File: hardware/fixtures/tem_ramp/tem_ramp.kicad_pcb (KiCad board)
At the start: 2 copper layers, 100 x 59 mm, 0 parts

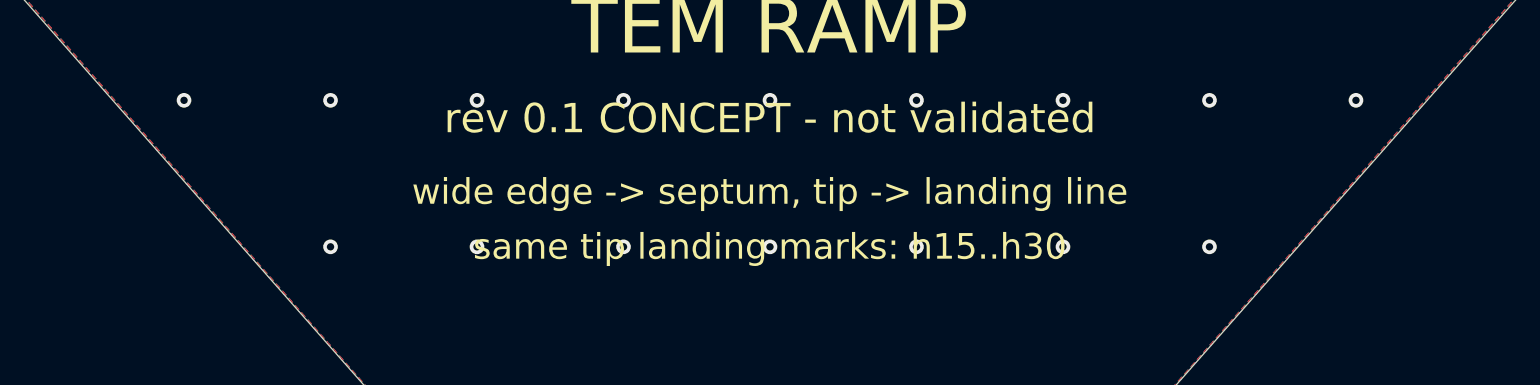
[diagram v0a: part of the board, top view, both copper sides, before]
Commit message: First fixture session: TEM cell sees the implant at every placement
TEM cell (h = 20 mm): the implanted Nano X shows a ~1 dB, ~40 MHz wide
notch at 1171 MHz at every placement and both orientations (sim: -1.2 dB
at 1185 MHz). Six of seven genuine placements stay within 0.2 dB; one
genuine re-check showed a similar notch near 1230 MHz, cause unknown.
Slot line: a small (-0.13..-0.20 dB) dip at 817-861 MHz at 0 deg only.

Also:
- gen_fixtures.py: TEM landing marks now place the ramp tip where the
  rigid ramp's tab actually lands, with the ramp overlapping the septum by
  4 mm; regenerated TEM boards and assembly step 3.
- nanovna_capture.py: zeros mean "outside the active calibration's span"
  (e.g. slot 1 recalled at power-on); say to `recall 0`.

Co-Authored-By: Claude Opus 5.5 <noreply@anthropic.com>
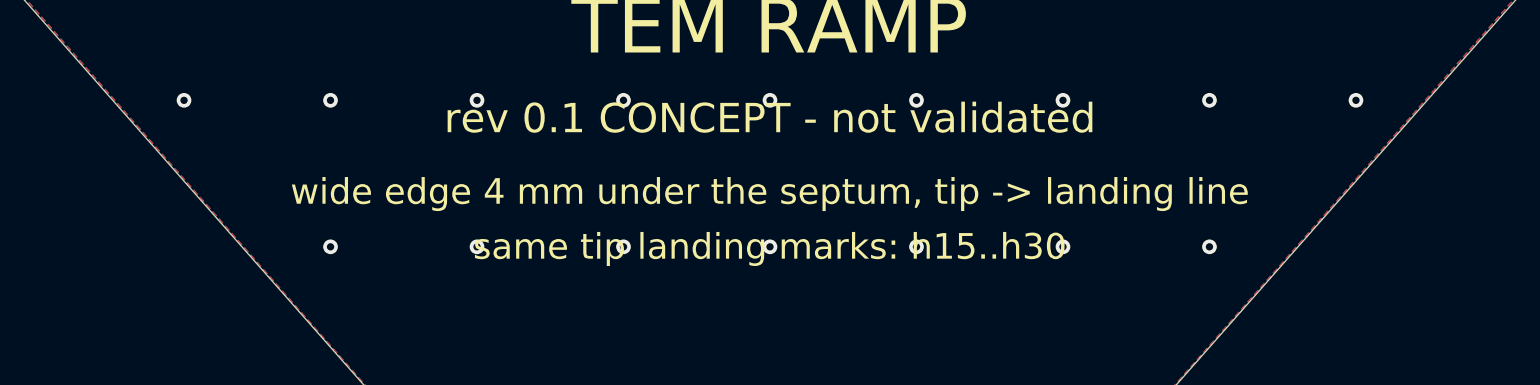
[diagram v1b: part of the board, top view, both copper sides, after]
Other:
- board text added: "wide edge 4 mm under the septum, tip -> landing line"
- board text removed: "wide edge -> septum, tip -> landing line"
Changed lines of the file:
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@@
 		(layer "Edge.Cuts")
 	)
-	(gr_text "wide edge -> septum, tip -> landing line"
+	(gr_text "wide edge 4 mm under the septum, tip -> landing line"
 		(at 150 171 0)
 		(layer "F.SilkS")
@@
 	)
 	(via
+		(at 158 174)
+		(size 0.8)
+		(drill 0.4)
+		(layers "F.Cu" "B.Cu")
+		(net "SEPTUM")
+	)
+	(via
+		(at 150 174)
+		(size 0.8)
+		(drill 0.4)
+		(layers "F.Cu" "B.Cu")
+		(net "SEPTUM")
+	)
+	(via
+		(at 126 158)
+		(size 0.8)
+		(drill 0.4)
+		(layers "F.Cu" "B.Cu")
+		(net "SEPTUM")
+	)
+	(via
+		(at 166 166)
+		(size 0.8)
+		(drill 0.4)
+		(layers "F.Cu" "B.Cu")
+		(net "SEPTUM")
+	)
+	(via
+		(at 166 182)
+		(size 0.8)
+		(drill 0.4)
+		(layers "F.Cu" "B.Cu")
+		(net "SEPTUM")
+	)
+	(via
+		(at 166 158)
+		(size 0.8)
+		(drill 0.4)
+		(layers "F.Cu" "B.Cu")
+		(net "SEPTUM")
+	)
+	(via
+		(at 158 166)
+		(size 0.8)
+		(drill 0.4)
+		(layers "F.Cu" "B.Cu")
+		(net "SEPTUM")
+	)
+	(via
+		(at 182 158)
+		(size 0.8)
+		(drill 0.4)
+		(layers "F.Cu" "B.Cu")
+		(net "SEPTUM")
+	)
+	(via
 		(at 126 174)
 		(size 0.8)
@@
 	)
 	(via
-		(at 182 158)
+		(at 134 182)
+		(size 0.8)
+		(drill 0.4)
+		(layers "F.Cu" "B.Cu")
+		(net "SEPTUM")
+	)
+	(via
+		(at 118 158)
+		(size 0.8)
+		(drill 0.4)
+		(layers "F.Cu" "B.Cu")
+		(net "SEPTUM")
+	)
+	(via
+		(at 190 158)
+		(size 0.8)
+		(drill 0.4)
+		(layers "F.Cu" "B.Cu")
+		(net "SEPTUM")
+	)
+	(via
+		(at 150 158)
+		(size 0.8)
+		(drill 0.4)
+		(layers "F.Cu" "B.Cu")
+		(net "SEPTUM")
+	)
+	(via
+		(at 142 166)
+		(size 0.8)
+		(drill 0.4)
+		(layers "F.Cu" "B.Cu")
+		(net "SEPTUM")
+	)
+	(via
+		(at 174 166)
 		(size 0.8)
 		(drill 0.4)
@@
 	)
 	(via
+		(at 142 190)
+		(size 0.8)
+		(drill 0.4)
+		(layers "F.Cu" "B.Cu")
+		(net "SEPTUM")
+	)
+	(via
+		(at 118 166)
+		(size 0.8)
+		(drill 0.4)
+		(layers "F.Cu" "B.Cu")
+		(net "SEPTUM")
+	)
+	(via
+		(at 134 166)
+		(size 0.8)
+		(drill 0.4)
+		(layers "F.Cu" "B.Cu")
+		(net "SEPTUM")
+	)
+	(via
+		(at 158 158)
+		(size 0.8)
+		(drill 0.4)
+		(layers "F.Cu" "B.Cu")
+		(net "SEPTUM")
+	)
+	(via
+		(at 158 182)
+		(size 0.8)
+		(drill 0.4)
+		(layers "F.Cu" "B.Cu")
+		(net "SEPTUM")
+	)
+	(via
 		(at 150 182)
 		(size 0.8)
@@
 	)
 	(via
+		(at 142 158)
+		(size 0.8)
+		(drill 0.4)
+		(layers "F.Cu" "B.Cu")
+		(net "SEPTUM")
+	)
+	(via
+		(at 150 198)
+		(size 0.8)
+		(drill 0.4)
+		(layers "F.Cu" "B.Cu")
+		(net "SEPTUM")
+	)
+	(via
+		(at 134 174)
+		(size 0.8)
+		(drill 0.4)
+		(layers "F.Cu" "B.Cu")
+		(net "SEPTUM")
+	)
+	(via
+		(at 166 174)
+		(size 0.8)
+		(drill 0.4)
+		(layers "F.Cu" "B.Cu")
+		(net "SEPTUM")
+	)
+	(via
+		(at 110 158)
+		(size 0.8)
+		(drill 0.4)
+		(layers "F.Cu" "B.Cu")
+		(net "SEPTUM")
+	)
+	(via
+		(at 142 182)
+		(size 0.8)
+		(drill 0.4)
+		(layers "F.Cu" "B.Cu")
+		(net "SEPTUM")
+	)
+	(via
+		(at 174 174)
+		(size 0.8)
+		(drill 0.4)
+		(layers "F.Cu" "B.Cu")
+		(net "SEPTUM")
+	)
+	(via
+		(at 150 190)
+		(size 0.8)
+		(drill 0.4)
+		(layers "F.Cu" "B.Cu")
+		(net "SEPTUM")
+	)
+	(via
+		(at 158 190)
+		(size 0.8)
+		(drill 0.4)
+		(layers "F.Cu" "B.Cu")
+		(net "SEPTUM")
+	)
+	(via
+		(at 182 166)
+		(size 0.8)
+		(drill 0.4)
+		(layers "F.Cu" "B.Cu")
+		(net "SEPTUM")
+	)
+	(via
 		(at 142 174)
 		(size 0.8)
@@
 	)
 	(via
-		(at 166 166)
-		(size 0.8)
-		(drill 0.4)
-		(layers "F.Cu" "B.Cu")
-		(net "SEPTUM")
-	)
-	(via
-		(at 182 166)
-		(size 0.8)
-		(drill 0.4)
-		(layers "F.Cu" "B.Cu")
-		(net "SEPTUM")
-	)
-	(via
-		(at 174 174)
-		(size 0.8)
-		(drill 0.4)
-		(layers "F.Cu" "B.Cu")
-		(net "SEPTUM")
-	)
-	(via
-		(at 142 158)
-		(size 0.8)
-		(drill 0.4)
-		(layers "F.Cu" "B.Cu")
-		(net "SEPTUM")
-	)
-	(via
-		(at 134 166)
-		(size 0.8)
-		(drill 0.4)
-		(layers "F.Cu" "B.Cu")
-		(net "SEPTUM")
-	)
-	(via
-		(at 150 158)
-		(size 0.8)
-		(drill 0.4)
-		(layers "F.Cu" "B.Cu")
-		(net "SEPTUM")
-	)
-	(via
-		(at 142 166)
-		(size 0.8)
-		(drill 0.4)
-		(layers "F.Cu" "B.Cu")
-		(net "SEPTUM")
-	)
-	(via
-		(at 158 166)
-		(size 0.8)
-		(drill 0.4)
-		(layers "F.Cu" "B.Cu")
-		(net "SEPTUM")
-	)
-	(via
-		(at 142 182)
-		(size 0.8)
-		(drill 0.4)
-		(layers "F.Cu" "B.Cu")
-		(net "SEPTUM")
-	)
-	(via
-		(at 150 190)
-		(size 0.8)
-		(drill 0.4)
-		(layers "F.Cu" "B.Cu")
-		(net "SEPTUM")
-	)
-	(via
 		(at 126 166)
 		(size 0.8)
@@
 	)
 	(via
-		(at 150 198)
-		(size 0.8)
-		(drill 0.4)
-		(layers "F.Cu" "B.Cu")
-		(net "SEPTUM")
-	)
-	(via
-		(at 118 166)
-		(size 0.8)
-		(drill 0.4)
-		(layers "F.Cu" "B.Cu")
-		(net "SEPTUM")
-	)
-	(via
-		(at 158 174)
-		(size 0.8)
-		(drill 0.4)
-		(layers "F.Cu" "B.Cu")
-		(net "SEPTUM")
-	)
-	(via
-		(at 158 182)
-		(size 0.8)
-		(drill 0.4)
-		(layers "F.Cu" "B.Cu")
-		(net "SEPTUM")
-	)
-	(via
-		(at 158 190)
-		(size 0.8)
-		(drill 0.4)
-		(layers "F.Cu" "B.Cu")
-		(net "SEPTUM")
-	)
-	(via
-		(at 110 158)
-		(size 0.8)
-		(drill 0.4)
-		(layers "F.Cu" "B.Cu")
-		(net "SEPTUM")
-	)
-	(via
-		(at 134 174)
-		(size 0.8)
-		(drill 0.4)
-		(layers "F.Cu" "B.Cu")
-		(net "SEPTUM")
-	)
-	(via
-		(at 142 190)
-		(size 0.8)
-		(drill 0.4)
-		(layers "F.Cu" "B.Cu")
-		(net "SEPTUM")
-	)
-	(via
-		(at 134 182)
-		(size 0.8)
-		(drill 0.4)
-		(layers "F.Cu" "B.Cu")
-		(net "SEPTUM")
-	)
-	(via
-		(at 166 158)
-		(size 0.8)
-		(drill 0.4)
-		(layers "F.Cu" "B.Cu")
-		(net "SEPTUM")
-	)
-	(via
-		(at 126 158)
-		(size 0.8)
-		(drill 0.4)
-		(layers "F.Cu" "B.Cu")
-		(net "SEPTUM")
-	)
-	(via
-		(at 158 158)
-		(size 0.8)
-		(drill 0.4)
-		(layers "F.Cu" "B.Cu")
-		(net "SEPTUM")
-	)
-	(via
-		(at 190 158)
-		(size 0.8)
-		(drill 0.4)
-		(layers "F.Cu" "B.Cu")
-		(net "SEPTUM")
-	)
-	(via
-		(at 166 182)
-		(size 0.8)
-		(drill 0.4)
-		(layers "F.Cu" "B.Cu")
-		(net "SEPTUM")
-	)
-	(via
-		(at 150 174)
+		(at 150 166)
 		(size 0.8)
 		(drill 0.4)
@@
 		(size 0.8)
 		(drill 0.4)
-		(layers "F.Cu" "B.Cu")
-		(net "SEPTUM")
-	)
-	(via
-		(at 150 166)
-		(size 0.8)
-		(drill 0.4)
-		(layers "F.Cu" "B.Cu")
-		(net "SEPTUM")
-	)
-	(via
-		(at 174 166)
-		(size 0.8)
-		(drill 0.4)
-		(layers "F.Cu" "B.Cu")
-		(net "SEPTUM")
-	)
-	(via
-		(at 118 158)
-		(size 0.8)
-		(drill 0.4)
-		(layers "F.Cu" "B.Cu")
-		(net "SEPTUM")
-	)
-	(via
-		(at 166 174)
-		(size 0.8)
-		(drill 0.4)
